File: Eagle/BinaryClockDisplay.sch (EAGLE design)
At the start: 45 parts

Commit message: Updated circuit board
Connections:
- removed net N$24: JP1.11, JP2.8
- removed net N$25: JP1.12, JP2.10
- removed net N$27: JP1.13, JP2.12
- removed net N$28: JP1.14, JP2.16
- new net DATA4-GPIO12: JP1.11, JP2.32
- new net DATA5-GPIO16: JP1.12, JP2.36
- new net DATA6-GPIO20: JP1.13, JP2.38
- new net DATA7-GPIO21: JP1.14, JP2.40
- new net E-GPIO15: JP1.6, JP2.10
- new net RS-GPIO14: JP1.4, JP2.8
- net GND: now also JP1.3
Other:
- moved on the sheet: R1
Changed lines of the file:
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@@
 <attribute name="VALUE" x="238.76" y="55.88" size="1.778" layer="96" rot="R180"/>
 </instance>
-<instance part="R1" gate="G$1" x="238.76" y="10.16" smashed="yes" rot="R180">
-<attribute name="NAME" x="242.57" y="8.6614" size="1.778" layer="95" rot="R180"/>
-<attribute name="VALUE" x="242.57" y="13.462" size="1.778" layer="96" rot="R180"/>
+<instance part="R1" gate="G$1" x="243.84" y="0" smashed="yes" rot="R270">
+<attribute name="NAME" x="245.3386" y="3.81" size="1.778" layer="95" rot="R270"/>
 </instance>
 </instances>
@@
 <pinref part="GND23" gate="1" pin="GND"/>
 <wire x1="236.22" y1="45.72" x2="236.22" y2="50.8" width="0.1524" layer="91"/>
+<junction x="236.22" y="45.72"/>
+<pinref part="JP1" gate="A" pin="3"/>
+<wire x1="236.22" y1="40.64" x2="236.22" y2="45.72" width="0.1524" layer="91"/>
+<wire x1="254" y1="40.64" x2="236.22" y2="40.64" width="0.1524" layer="91"/>
 <pinref part="JP1" gate="A" pin="5"/>
 <wire x1="254" y1="35.56" x2="236.22" y2="35.56" width="0.1524" layer="91"/>
-<wire x1="236.22" y1="35.56" x2="236.22" y2="45.72" width="0.1524" layer="91"/>
-<junction x="236.22" y="45.72"/>
+<wire x1="236.22" y1="35.56" x2="236.22" y2="40.64" width="0.1524" layer="91"/>
+<junction x="236.22" y="40.64"/>
 </segment>
 </net>
@@
 <pinref part="JP2" gate="A" pin="4"/>
 <pinref part="JP1" gate="A" pin="2"/>
-<wire x1="218.44" y1="43.18" x2="233.68" y2="43.18" width="0.1524" layer="91"/>
 <label x="226.06" y="45.72" size="1.778" layer="95"/>
+<wire x1="218.44" y1="43.18" x2="254" y2="43.18" width="0.1524" layer="91"/>
+</segment>
+<segment>
 <pinref part="R1" gate="G$1" pin="2"/>
-<wire x1="233.68" y1="43.18" x2="254" y2="43.18" width="0.1524" layer="91"/>
-<wire x1="233.68" y1="10.16" x2="233.68" y2="43.18" width="0.1524" layer="91"/>
-<junction x="233.68" y="43.18"/>
-</segment>
-</net>
-<net name="N$9" class="0">
-<segment>
-<pinref part="JP1" gate="A" pin="15"/>
-<pinref part="R1" gate="G$1" pin="1"/>
-<wire x1="254" y1="10.16" x2="243.84" y2="10.16" width="0.1524" layer="91"/>
-</segment>
-</net>
-<net name="N$24" class="0">
+<wire x1="243.84" y1="-5.08" x2="243.84" y2="-7.62" width="0.1524" layer="91"/>
+<label x="246.38" y="-7.62" size="1.778" layer="95"/>
+</segment>
+</net>
+<net name="RS-GPIO14" class="0">
+<segment>
+<pinref part="JP2" gate="A" pin="8"/>
+<pinref part="JP1" gate="A" pin="4"/>
+<wire x1="218.44" y1="38.1" x2="254" y2="38.1" width="0.1524" layer="91"/>
+<label x="236.22" y="38.1" size="1.778" layer="95"/>
+</segment>
+</net>
+<net name="E-GPIO15" class="0">
+<segment>
+<pinref part="JP1" gate="A" pin="6"/>
+<wire x1="254" y1="33.02" x2="226.06" y2="33.02" width="0.1524" layer="91"/>
+<wire x1="226.06" y1="33.02" x2="226.06" y2="35.56" width="0.1524" layer="91"/>
+<pinref part="JP2" gate="A" pin="10"/>
+<wire x1="226.06" y1="35.56" x2="218.44" y2="35.56" width="0.1524" layer="91"/>
+<label x="236.22" y="33.02" size="1.778" layer="95"/>
+</segment>
+</net>
+<net name="DATA4-GPIO12" class="0">
 <segment>
 <pinref part="JP1" gate="A" pin="11"/>
-<wire x1="254" y1="20.32" x2="231.14" y2="20.32" width="0.1524" layer="91"/>
-<wire x1="231.14" y1="20.32" x2="231.14" y2="38.1" width="0.1524" layer="91"/>
-<pinref part="JP2" gate="A" pin="8"/>
-<wire x1="231.14" y1="38.1" x2="218.44" y2="38.1" width="0.1524" layer="91"/>
-</segment>
-</net>
-<net name="N$25" class="0">
+<wire x1="254" y1="20.32" x2="226.06" y2="20.32" width="0.1524" layer="91"/>
+<wire x1="226.06" y1="20.32" x2="226.06" y2="7.62" width="0.1524" layer="91"/>
+<pinref part="JP2" gate="A" pin="32"/>
+<wire x1="226.06" y1="7.62" x2="218.44" y2="7.62" width="0.1524" layer="91"/>
+<label x="231.14" y="20.32" size="1.778" layer="95"/>
+</segment>
+</net>
+<net name="DATA5-GPIO16" class="0">
 <segment>
 <pinref part="JP1" gate="A" pin="12"/>
 <wire x1="254" y1="17.78" x2="228.6" y2="17.78" width="0.1524" layer="91"/>
-<pinref part="JP2" gate="A" pin="10"/>
-<wire x1="228.6" y1="17.78" x2="228.6" y2="35.56" width="0.1524" layer="91"/>
-<wire x1="228.6" y1="35.56" x2="218.44" y2="35.56" width="0.1524" layer="91"/>
-</segment>
-</net>
-<net name="N$27" class="0">
-<segment>
+<wire x1="228.6" y1="17.78" x2="228.6" y2="2.54" width="0.1524" layer="91"/>
+<pinref part="JP2" gate="A" pin="36"/>
+<wire x1="228.6" y1="2.54" x2="218.44" y2="2.54" width="0.1524" layer="91"/>
+<label x="231.14" y="17.78" size="1.778" layer="95"/>
+</segment>
+</net>
+<net name="DATA6-GPIO20" class="0">
+<segment>
+<pinref part="JP2" gate="A" pin="38"/>
+<wire x1="218.44" y1="0" x2="231.14" y2="0" width="0.1524" layer="91"/>
+<wire x1="231.14" y1="0" x2="231.14" y2="15.24" width="0.1524" layer="91"/>
 <pinref part="JP1" gate="A" pin="13"/>
-<wire x1="254" y1="15.24" x2="226.06" y2="15.24" width="0.1524" layer="91"/>
-<wire x1="226.06" y1="15.24" x2="226.06" y2="33.02" width="0.1524" layer="91"/>
-<pinref part="JP2" gate="A" pin="12"/>
-<wire x1="226.06" y1="33.02" x2="218.44" y2="33.02" width="0.1524" layer="91"/>
-</segment>
-</net>
-<net name="N$28" class="0">
-<segment>
-<pinref part="JP2" gate="A" pin="16"/>
-<wire x1="218.44" y1="27.94" x2="223.52" y2="27.94" width="0.1524" layer="91"/>
-<wire x1="223.52" y1="27.94" x2="223.52" y2="12.7" width="0.1524" layer="91"/>
+<wire x1="231.14" y1="15.24" x2="254" y2="15.24" width="0.1524" layer="91"/>
+<label x="231.14" y="15.24" size="1.778" layer="95"/>
+</segment>
+</net>
+<net name="DATA7-GPIO21" class="0">
+<segment>
 <pinref part="JP1" gate="A" pin="14"/>
-<wire x1="223.52" y1="12.7" x2="254" y2="12.7" width="0.1524" layer="91"/>
-</segment>
-</net>
+<wire x1="254" y1="12.7" x2="233.68" y2="12.7" width="0.1524" layer="91"/>
+<wire x1="233.68" y1="12.7" x2="233.68" y2="-2.54" width="0.1524" layer="91"/>
+<pinref part="JP2" gate="A" pin="40"/>
+<wire x1="233.68" y1="-2.54" x2="218.44" y2="-2.54" width="0.1524" layer="91"/>
+<label x="231.14" y="12.7" size="1.778" layer="95"/>
+</segment>
+</net>
+<net name="N$9" class="0">
+<segment>
+<pinref part="JP1" gate="A" pin="15"/>
+<wire x1="254" y1="10.16" x2="243.84" y2="10.16" width="0.1524" layer="91"/>
+<pinref part="R1" gate="G$1" pin="1"/>
+<wire x1="243.84" y1="10.16" x2="243.84" y2="5.08" width="0.1524" layer="91"/>
+</segment>
+</net>

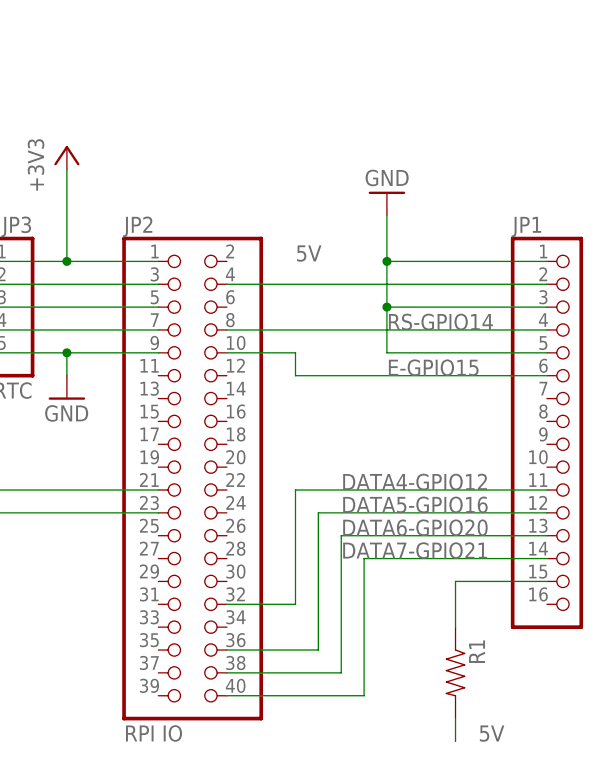
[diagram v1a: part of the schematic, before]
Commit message: Simplyfied design
I decided to simmplify the design and make this a pure binary clock. Therefore I removed the interface to the 1602 display. I will look a bit cooler as binary only ;-)
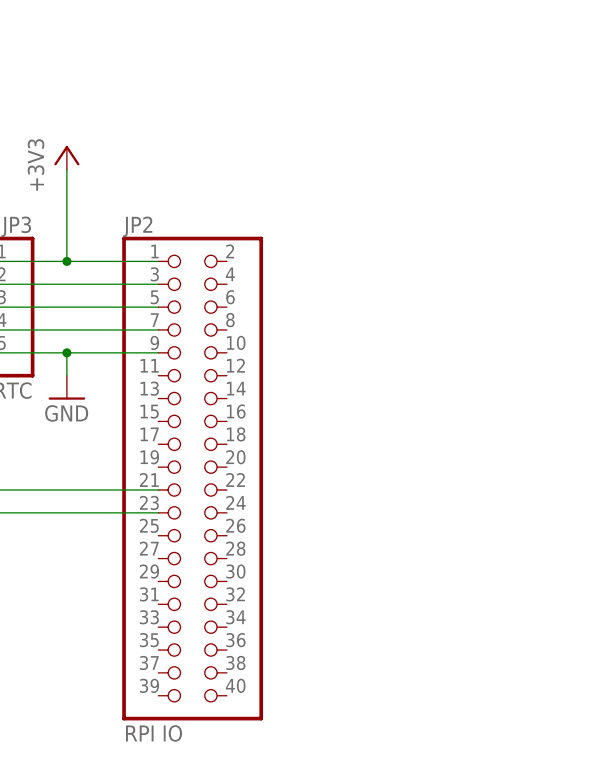
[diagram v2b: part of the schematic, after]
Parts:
- removed JP1: 1602A, pinhead:PINHD-1X16
- removed R1: 1k, SparkFun-Resistors:RESISTOR0805-RES
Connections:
- removed net 5V: JP1.2, JP2.4, R1.2
- removed net DATA4-GPIO12: JP1.11, JP2.32
- removed net DATA5-GPIO16: JP1.12, JP2.36
- removed net DATA6-GPIO20: JP1.13, JP2.38
- removed net DATA7-GPIO21: JP1.14, JP2.40
- removed net E-GPIO15: JP1.6, JP2.10
- removed net N$9: JP1.15, R1.1
- removed net RS-GPIO14: JP1.4, JP2.8
- net GND: no longer JP1.1, JP1.3, JP1.5
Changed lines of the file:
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@@
 <parts>
 <part name="D1" library="SparkFun-LED" library_urn="urn:adsk.eagle:library:529" deviceset="WS2812B" device="" package3d_urn="urn:adsk.eagle:package:39369/1" value="WS2812B"/>
-<part name="JP1" library="pinhead" library_urn="urn:adsk.eagle:library:325" deviceset="PINHD-1X16" device="" package3d_urn="urn:adsk.eagle:package:22432/2" value="1602A"/>
 <part name="JP2" library="pinhead" library_urn="urn:adsk.eagle:library:325" deviceset="PINHD-2X20" device="" package3d_urn="urn:adsk.eagle:package:22443/2" value="RPI IO"/>
 <part name="C4" library="SparkFun-Passives" deviceset="CAP" device="0805" value="100nF"/>
@@
 <part name="S1" library="SparkFun-Electromechanical" deviceset="SWITCH-MOMENTARY-2" device="SMD-1101NE" value="SWITCH"/>
 <part name="GND22" library="supply1" deviceset="GND" device=""/>
-<part name="GND23" library="supply1" deviceset="GND" device=""/>
-<part name="R1" library="SparkFun-Resistors" deviceset="RESISTOR" device="0805-RES" value="1k"/>
 </parts>
 <sheets>
@@
 <attribute name="VALUE" x="116.84" y="27.94" size="1.778" layer="95"/>
 </instance>
-<instance part="JP1" gate="A" x="256.54" y="27.94" smashed="yes">
-<attribute name="NAME" x="250.19" y="48.895" size="1.778" layer="95"/>
-</instance>
 <instance part="JP2" gate="A" x="213.36" y="22.86" smashed="yes">
 <attribute name="NAME" x="207.01" y="48.895" size="1.778" layer="95"/>
@@
 <instance part="GND22" gate="1" x="129.54" y="12.7" smashed="yes">
 <attribute name="VALUE" x="127" y="10.16" size="1.778" layer="96"/>
-</instance>
-<instance part="GND23" gate="1" x="236.22" y="53.34" smashed="yes" rot="R180">
-<attribute name="VALUE" x="238.76" y="55.88" size="1.778" layer="96" rot="R180"/>
-</instance>
-<instance part="R1" gate="G$1" x="243.84" y="0" smashed="yes" rot="R270">
-<attribute name="NAME" x="245.3386" y="3.81" size="1.778" layer="95" rot="R270"/>
 </instance>
 </instances>
@@
 <wire x1="134.62" y1="17.78" x2="129.54" y2="17.78" width="0.1524" layer="91"/>
 <wire x1="129.54" y1="17.78" x2="129.54" y2="15.24" width="0.1524" layer="91"/>
-</segment>
-<segment>
-<pinref part="JP1" gate="A" pin="1"/>
-<wire x1="254" y1="45.72" x2="236.22" y2="45.72" width="0.1524" layer="91"/>
-<pinref part="GND23" gate="1" pin="GND"/>
-<wire x1="236.22" y1="45.72" x2="236.22" y2="50.8" width="0.1524" layer="91"/>
-<junction x="236.22" y="45.72"/>
-<pinref part="JP1" gate="A" pin="3"/>
-<wire x1="236.22" y1="40.64" x2="236.22" y2="45.72" width="0.1524" layer="91"/>
-<wire x1="254" y1="40.64" x2="236.22" y2="40.64" width="0.1524" layer="91"/>
-<pinref part="JP1" gate="A" pin="5"/>
-<wire x1="254" y1="35.56" x2="236.22" y2="35.56" width="0.1524" layer="91"/>
-<wire x1="236.22" y1="35.56" x2="236.22" y2="40.64" width="0.1524" layer="91"/>
-<junction x="236.22" y="40.64"/>
 </segment>
 </net>
@@
 </segment>
 </net>
-<net name="5V" class="0">
-<segment>
-<pinref part="JP2" gate="A" pin="4"/>
-<pinref part="JP1" gate="A" pin="2"/>
-<label x="226.06" y="45.72" size="1.778" layer="95"/>
-<wire x1="218.44" y1="43.18" x2="254" y2="43.18" width="0.1524" layer="91"/>
-</segment>
-<segment>
-<pinref part="R1" gate="G$1" pin="2"/>
-<wire x1="243.84" y1="-5.08" x2="243.84" y2="-7.62" width="0.1524" layer="91"/>
-<label x="246.38" y="-7.62" size="1.778" layer="95"/>
-</segment>
-</net>
-<net name="RS-GPIO14" class="0">
-<segment>
-<pinref part="JP2" gate="A" pin="8"/>
-<pinref part="JP1" gate="A" pin="4"/>
-<wire x1="218.44" y1="38.1" x2="254" y2="38.1" width="0.1524" layer="91"/>
-<label x="236.22" y="38.1" size="1.778" layer="95"/>
-</segment>
-</net>
-<net name="E-GPIO15" class="0">
-<segment>
-<pinref part="JP1" gate="A" pin="6"/>
-<wire x1="254" y1="33.02" x2="226.06" y2="33.02" width="0.1524" layer="91"/>
-<wire x1="226.06" y1="33.02" x2="226.06" y2="35.56" width="0.1524" layer="91"/>
-<pinref part="JP2" gate="A" pin="10"/>
-<wire x1="226.06" y1="35.56" x2="218.44" y2="35.56" width="0.1524" layer="91"/>
-<label x="236.22" y="33.02" size="1.778" layer="95"/>
-</segment>
-</net>
-<net name="DATA4-GPIO12" class="0">
-<segment>
-<pinref part="JP1" gate="A" pin="11"/>
-<wire x1="254" y1="20.32" x2="226.06" y2="20.32" width="0.1524" layer="91"/>
-<wire x1="226.06" y1="20.32" x2="226.06" y2="7.62" width="0.1524" layer="91"/>
-<pinref part="JP2" gate="A" pin="32"/>
-<wire x1="226.06" y1="7.62" x2="218.44" y2="7.62" width="0.1524" layer="91"/>
-<label x="231.14" y="20.32" size="1.778" layer="95"/>
-</segment>
-</net>
-<net name="DATA5-GPIO16" class="0">
-<segment>
-<pinref part="JP1" gate="A" pin="12"/>
-<wire x1="254" y1="17.78" x2="228.6" y2="17.78" width="0.1524" layer="91"/>
-<wire x1="228.6" y1="17.78" x2="228.6" y2="2.54" width="0.1524" layer="91"/>
-<pinref part="JP2" gate="A" pin="36"/>
-<wire x1="228.6" y1="2.54" x2="218.44" y2="2.54" width="0.1524" layer="91"/>
-<label x="231.14" y="17.78" size="1.778" layer="95"/>
-</segment>
-</net>
-<net name="DATA6-GPIO20" class="0">
-<segment>
-<pinref part="JP2" gate="A" pin="38"/>
-<wire x1="218.44" y1="0" x2="231.14" y2="0" width="0.1524" layer="91"/>
-<wire x1="231.14" y1="0" x2="231.14" y2="15.24" width="0.1524" layer="91"/>
-<pinref part="JP1" gate="A" pin="13"/>
-<wire x1="231.14" y1="15.24" x2="254" y2="15.24" width="0.1524" layer="91"/>
-<label x="231.14" y="15.24" size="1.778" layer="95"/>
-</segment>
-</net>
-<net name="DATA7-GPIO21" class="0">
-<segment>
-<pinref part="JP1" gate="A" pin="14"/>
-<wire x1="254" y1="12.7" x2="233.68" y2="12.7" width="0.1524" layer="91"/>
-<wire x1="233.68" y1="12.7" x2="233.68" y2="-2.54" width="0.1524" layer="91"/>
-<pinref part="JP2" gate="A" pin="40"/>
-<wire x1="233.68" y1="-2.54" x2="218.44" y2="-2.54" width="0.1524" layer="91"/>
-<label x="231.14" y="12.7" size="1.778" layer="95"/>
-</segment>
-</net>
-<net name="N$9" class="0">
-<segment>
-<pinref part="JP1" gate="A" pin="15"/>
-<wire x1="254" y1="10.16" x2="243.84" y2="10.16" width="0.1524" layer="91"/>
-<pinref part="R1" gate="G$1" pin="1"/>
-<wire x1="243.84" y1="10.16" x2="243.84" y2="5.08" width="0.1524" layer="91"/>
-</segment>
-</net>
